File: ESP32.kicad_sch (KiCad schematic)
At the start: 5 parts, among them U1 ESP32-S3-MINI-1-N8

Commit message: Create PCB
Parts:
- C1: value 1F -> 1uF; DigiKey_Part_Number (none) -> 311-1445-1-ND; Manufacturer_Part_Number (none) -> CC0603KRX5R8BB105; Price (none) -> €0.95
- C2: DigiKey_Part_Number (none) -> 311-1341-1-ND; Manufacturer_Part_Number (none) -> CC0603KRX7R8BB104; Price (none) -> €0.48
- C3: footprint Capacitor_SMD:C_0603_1608Metric -> Capacitor_SMD:C_0805_2012Metric; DigiKey_Part_Number (none) -> 311-1190-1-ND; Manufacturer_Part_Number (none) -> CC0805ZKY5V6BB335; Price (none) -> €0.17
- R1: footprint Resistor_SMD:R_0603_1608Metric -> Resistor_SMD:R_0402_1005Metric; DigiKey_Part_Number (none) -> 311-10KJRCT-ND; Manufacturer_Part_Number (none) -> RC0402JR-0710KL; Price (none) -> €0.30
- U1: Check_prices https://www.snapeda.com/parts/ESP32-S3-MINI-1-N8/Espressif+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 -> (none); Description_1 Bluetooth, WiFi 802.11b/g/n, Bluetooth v5.0 Transceiver Mod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 -> (none); DigiKey_Part_Number 1965-ESP32-S3-MINI-1-N8TR-ND -> 1965-ESP32-S3-MINI-1-N8CT-ND; MANUFACTURER Espressif -> (none); MAXIMUM_PACKAGE_HEIGHT 2.55mm -> (none); MF Espressif Systems -> (none); MP ESP32-S3-MINI-1-N8 -> (none); Manufacturer_Part_Number (none) -> ESP32-S3-MINI-1-N8; PARTREV v0.6 -> (none); Package None -> (none); Price (none) -> €5.03; STANDARD Manufacturer Recommendations -> (none); SnapEDA_Link https://www.snapeda.com/parts/ESP32-S3-MINI-1-N8/Espressif+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 -> (none)
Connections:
- net IO 19 renamed USB_N
- net IO 20 renamed USB_P
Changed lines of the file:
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@@
 		)
 	)
-	(global_label "IO 19"
+	(global_label "USB_N"
 		(shape input)
 		(at 66.04 40.64 0)
@@
 		)
 		(property "Intersheetrefs" "${INTERSHEET_REFS}"
-			(at 74.3471 40.64 0)
+			(at 75.1333 40.64 0)
 			(effects
 				(font
@@
 		)
 	)
-	(global_label "IO 20"
+	(global_label "USB_P"
 		(shape input)
 		(at 66.04 43.18 0)
@@
 		)
 		(property "Intersheetrefs" "${INTERSHEET_REFS}"
-			(at 74.3471 43.18 0)
+			(at 75.0728 43.18 0)
 			(effects
 				(font
@@
 		(dnp no)
 		(fields_autoplaced yes)
-		(property "Reference" "#PWR042"
+		(property "Reference" "#PWR01"
 			(at 29.21 17.78 0)
 			(effects
@@
 			(project "RFID_Device"
 				(path "/f4733a35-9ae9-40ca-bc69-86dc96557334/b59a840b-0db4-4dd4-af14-dad68e1751ca"
-					(reference "#PWR042")
+					(reference "#PWR01")
 					(unit 1)
 				)
@@
 			)
 		)
-		(property "Value" "1F"
+		(property "Value" "1uF"
 			(at 31.75 29.2035 0)
 			(effects
@@
 		)
 		(property "Description" "Unpolarized capacitor, small symbol"
+			(at 29.21 27.94 0)
+			(effects
+				(font
+					(size 1.27 1.27)
+				)
+				(hide yes)
+			)
+		)
+		(property "DigiKey_Part_Number" "311-1445-1-ND"
+			(at 29.21 27.94 0)
+			(effects
+				(font
+					(size 1.27 1.27)
+				)
+				(hide yes)
+			)
+		)
+		(property "Manufacturer_Part_Number" "CC0603KRX5R8BB105"
+			(at 29.21 27.94 0)
+			(effects
+				(font
+					(size 1.27 1.27)
+				)
+				(hide yes)
+			)
+		)
+		(property "Price" "€0.95"
 			(at 29.21 27.94 0)
 			(effects
@@
 			)
 		)
-		(property "Footprint" "Capacitor_SMD:C_0603_1608Metric"
+		(property "Footprint" "Capacitor_SMD:C_0805_2012Metric"
 			(at 80.01 24.13 0)
 			(effects
@@
 		)
 		(property "Description" "Unpolarized capacitor, small symbol"
+			(at 80.01 24.13 0)
+			(effects
+				(font
+					(size 1.27 1.27)
+				)
+				(hide yes)
+			)
+		)
+		(property "Price" "€0.17"
+			(at 80.01 24.13 0)
+			(effects
+				(font
+					(size 1.27 1.27)
+				)
+				(hide yes)
+			)
+		)
+		(property "DigiKey_Part_Number" "311-1190-1-ND"
+			(at 80.01 24.13 0)
+			(effects
+				(font
+					(size 1.27 1.27)
+				)
+				(hide yes)
+			)
+		)
+		(property "Manufacturer_Part_Number" "CC0805ZKY5V6BB335"
 			(at 80.01 24.13 0)
 			(effects
@@
 			)
 		)
-		(property "DigiKey_Part_Number" "1965-ESP32-S3-MINI-1-N8TR-ND"
+		(property "DigiKey_Part_Number" "1965-ESP32-S3-MINI-1-N8CT-ND"
 			(at 46.99 58.42 0)
 			(effects
@@
 			)
 		)
-		(property "SnapEDA_Link" "https://www.snapeda.com/parts/ESP32-S3-MINI-1-N8/Espressif+Systems/view-part/?ref=snap"
+		(property "Price" "€5.03"
 			(at 46.99 58.42 0)
 			(effects
@@
 					(size 1.27 1.27)
 				)
-				(justify bottom)
-				(hide yes)
-			)
-		)
-		(property "MAXIMUM_PACKAGE_HEIGHT" "2.55mm"
+			)
+		)
+		(property "Manufacturer_Part_Number" "ESP32-S3-MINI-1-N8"
 			(at 46.99 58.42 0)
 			(effects
@@
 					(size 1.27 1.27)
 				)
-				(justify bottom)
-				(hide yes)
-			)
-		)
-		(property "Package" "None"
-			(at 46.99 58.42 0)
-			(effects
-				(font
-					(size 1.27 1.27)
-				)
-				(justify bottom)
-				(hide yes)
-			)
-		)
-		(property "Check_prices" "https://www.snapeda.com/parts/ESP32-S3-MINI-1-N8/Espressif+Systems/view-part/?ref=eda"
-			(at 46.99 58.42 0)
-			(effects
-				(font
-					(size 1.27 1.27)
-				)
-				(justify bottom)
-				(hide yes)
-			)
-		)
-		(property "STANDARD" "Manufacturer Recommendations"
-			(at 46.99 58.42 0)
-			(effects
-				(font
-					(size 1.27 1.27)
-				)
-				(justify bottom)
-				(hide yes)
-			)
-		)
-		(property "PARTREV" "v0.6"
-			(at 46.99 58.42 0)
-			(effects
-				(font
-					(size 1.27 1.27)
-				)
-				(justify bottom)
-				(hide yes)
-			)
-		)
-		(property "MF" "Espressif Systems"
-			(at 46.99 58.42 0)
-			(effects
-				(font
-					(size 1.27 1.27)
-				)
-				(justify bottom)
-				(hide yes)
-			)
-		)
-		(property "MP" "ESP32-S3-MINI-1-N8"
-			(at 46.99 58.42 0)
-			(effects
-				(font
-					(size 1.27 1.27)
-				)
-				(justify bottom)
-				(hide yes)
-			)
-		)
-		(property "Description_1" "\n                        \n                            Bluetooth, WiFi 802.11b/g/n, Bluetooth v5.0 Transceiver Module 2.4GHz PCB Trace Surface Mount\n                        \n"
-			(at 46.99 58.42 0)
-			(effects
-				(font
-					(size 1.27 1.27)
-				)
-				(justify bottom)
-				(hide yes)
-			)
-		)
-		(property "MANUFACTURER" "Espressif"
-			(at 46.99 58.42 0)
-			(effects
-				(font
-					(size 1.27 1.27)
-				)
-				(justify bottom)
-				(hide yes)
 			)
 		)
@@
 			)
 		)
-		(property "Footprint" "Resistor_SMD:R_0603_1608Metric"
+		(property "Footprint" "Resistor_SMD:R_0402_1005Metric"
 			(at 25.4 33.02 0)
 			(effects
@@
 		)
 		(property "Description" "Resistor, small symbol"
+			(at 25.4 33.02 0)
+			(effects
+				(font
+					(size 1.27 1.27)
+				)
+				(hide yes)
+			)
+		)
+		(property "Price" "€0.30"
+			(at 25.4 33.02 0)
+			(effects
+				(font
+					(size 1.27 1.27)
+				)
+				(hide yes)
+			)
+		)
+		(property "DigiKey_Part_Number" "311-10KJRCT-ND"
+			(at 25.4 33.02 0)
+			(effects
+				(font
+					(size 1.27 1.27)
+				)
+				(hide yes)
+			)
+		)
+		(property "Manufacturer_Part_Number" "RC0402JR-0710KL"
 			(at 25.4 33.02 0)
 			(effects
@@
 			(at 69.85 24.13 0)
 			(effects
+				(font
+					(size 1.27 1.27)
+				)
+				(hide yes)
+			)
+		)
+		(property "DigiKey_Part_Number" "311-1341-1-ND"
+			(at 69.85 24.13 0)
+			(effects
+				(font
+					(size 1.27 1.27)
+				)
+				(hide yes)
+			)
+		)
+		(property "Price" "€0.48"
+			(at 69.85 24.13 0)
+			(effects
+				(font
+					(size 1.27 1.27)
+				)
+				(hide yes)
+			)
+		)
+		(property "Manufacturer_Part_Number" "CC0603KRX7R8BB104"
+			(at 69.85 24.13 0)
+			(effects

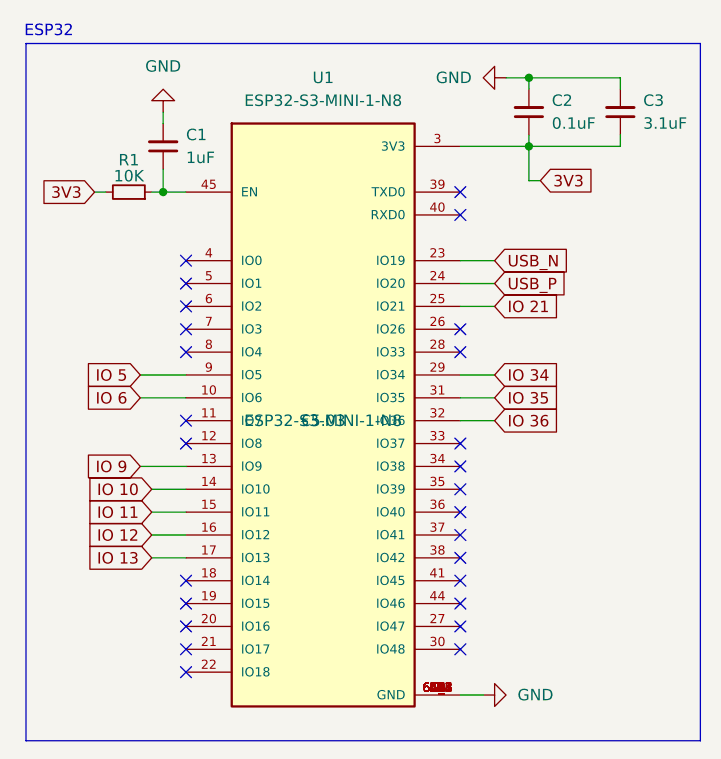
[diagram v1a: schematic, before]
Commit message: Fix minor design mistakes
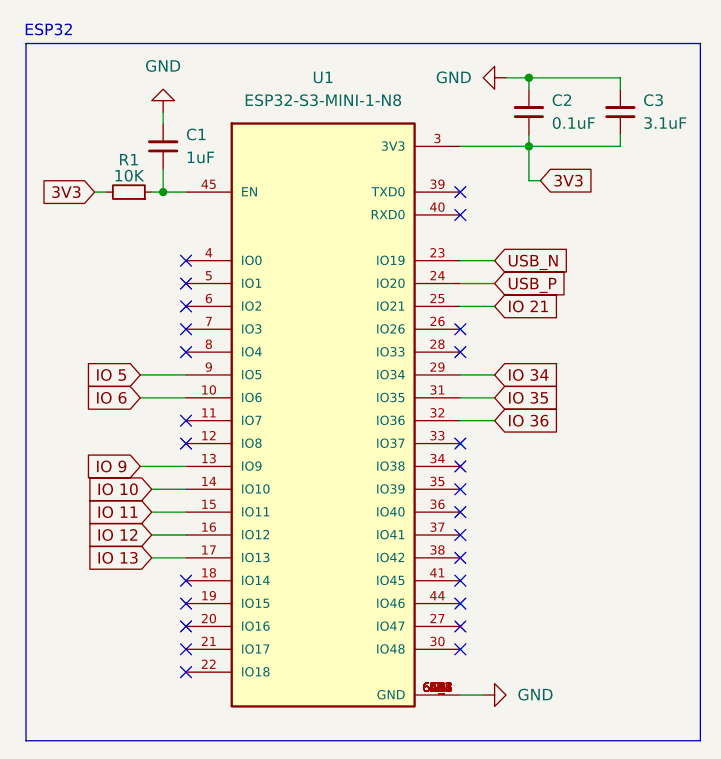
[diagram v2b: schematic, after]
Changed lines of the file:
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@@
 					(size 1.27 1.27)
 				)
+				(hide yes)
 			)
 		)
@@
 					(size 1.27 1.27)
 				)
+				(hide yes)
 			)
 		)
